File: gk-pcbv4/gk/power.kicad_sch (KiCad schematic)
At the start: 36 parts, among them J1 Conn_01x02, J2 Conn_01x02, Q1 DMN62D0U, Q2 2N7002, U1 STPMIC25B JC Module, U2 BQ24075RGT (_not_ BQ24075*T*R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, U3 MAX17048, U4 INA236[AB]IDDFR

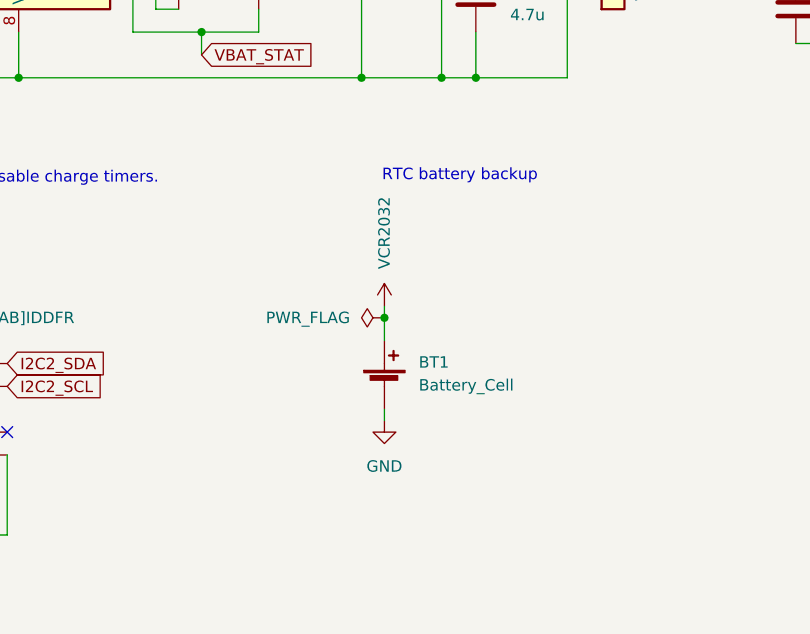
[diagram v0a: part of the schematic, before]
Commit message: add v2 controls board
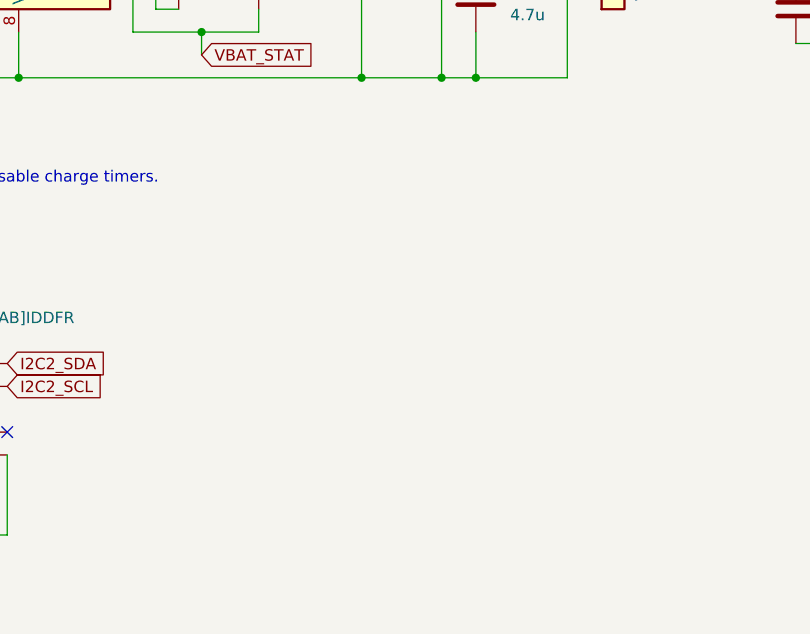
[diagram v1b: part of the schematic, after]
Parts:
- removed BT1: Battery_Cell, Battery:BatteryHolder_Keystone_3002_1x2032, symbol Device:Battery_Cell
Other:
- note removed: "RTC battery backup"

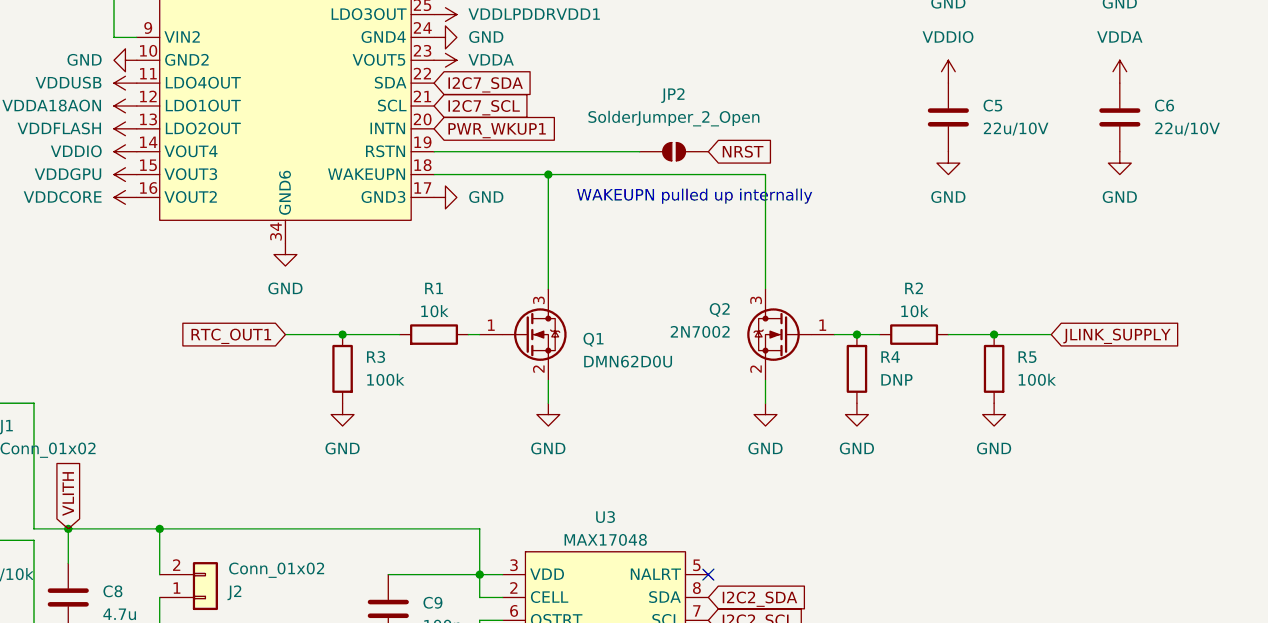
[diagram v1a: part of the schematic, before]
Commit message: Remove wakeupn mosfets in schematic
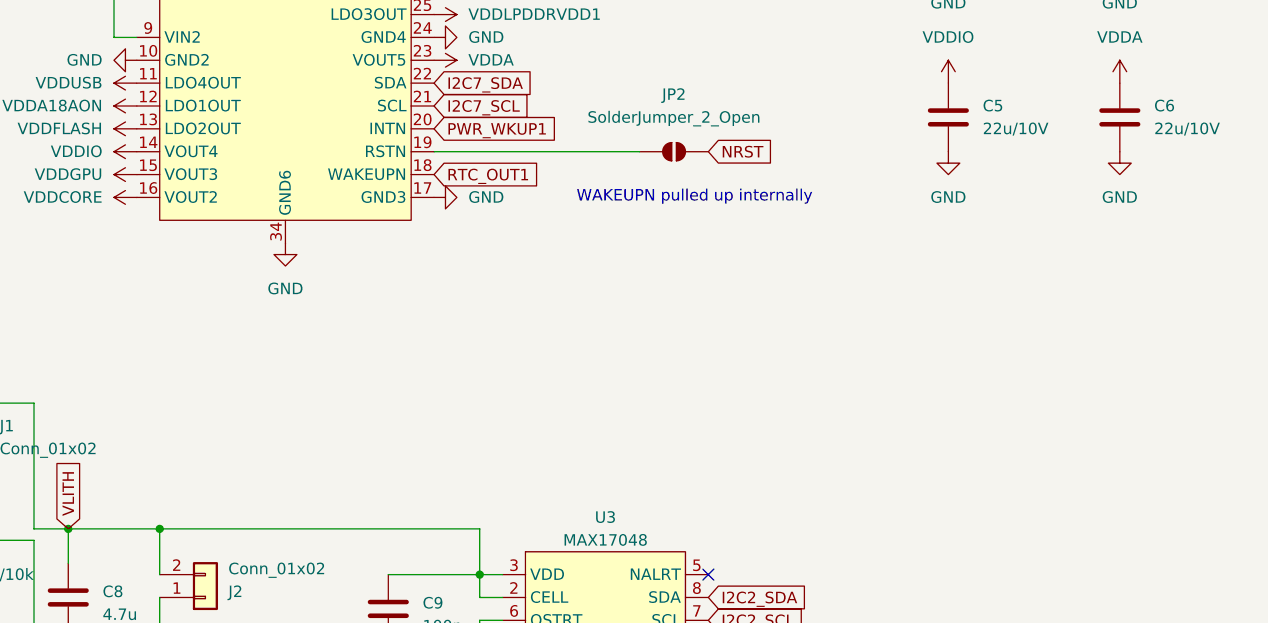
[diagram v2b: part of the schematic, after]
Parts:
- removed Q1: DMN62D0U, Package_TO_SOT_SMD:SOT-23, symbol Transistor_FET:2N7002
- removed Q2: 2N7002, Package_TO_SOT_SMD:SOT-23, symbol Transistor_FET:2N7002
- removed R1, R2: 10k, Resistor_SMD:R_0603_1608Metric, symbol Device:R
- removed R3, R5: 100k, Resistor_SMD:R_0603_1608Metric, symbol Device:R
- removed R4: DNP, Resistor_SMD:R_0603_1608Metric, symbol Device:R
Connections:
- net RTC_OUT1: now also U1.18 (WAKEUPN)

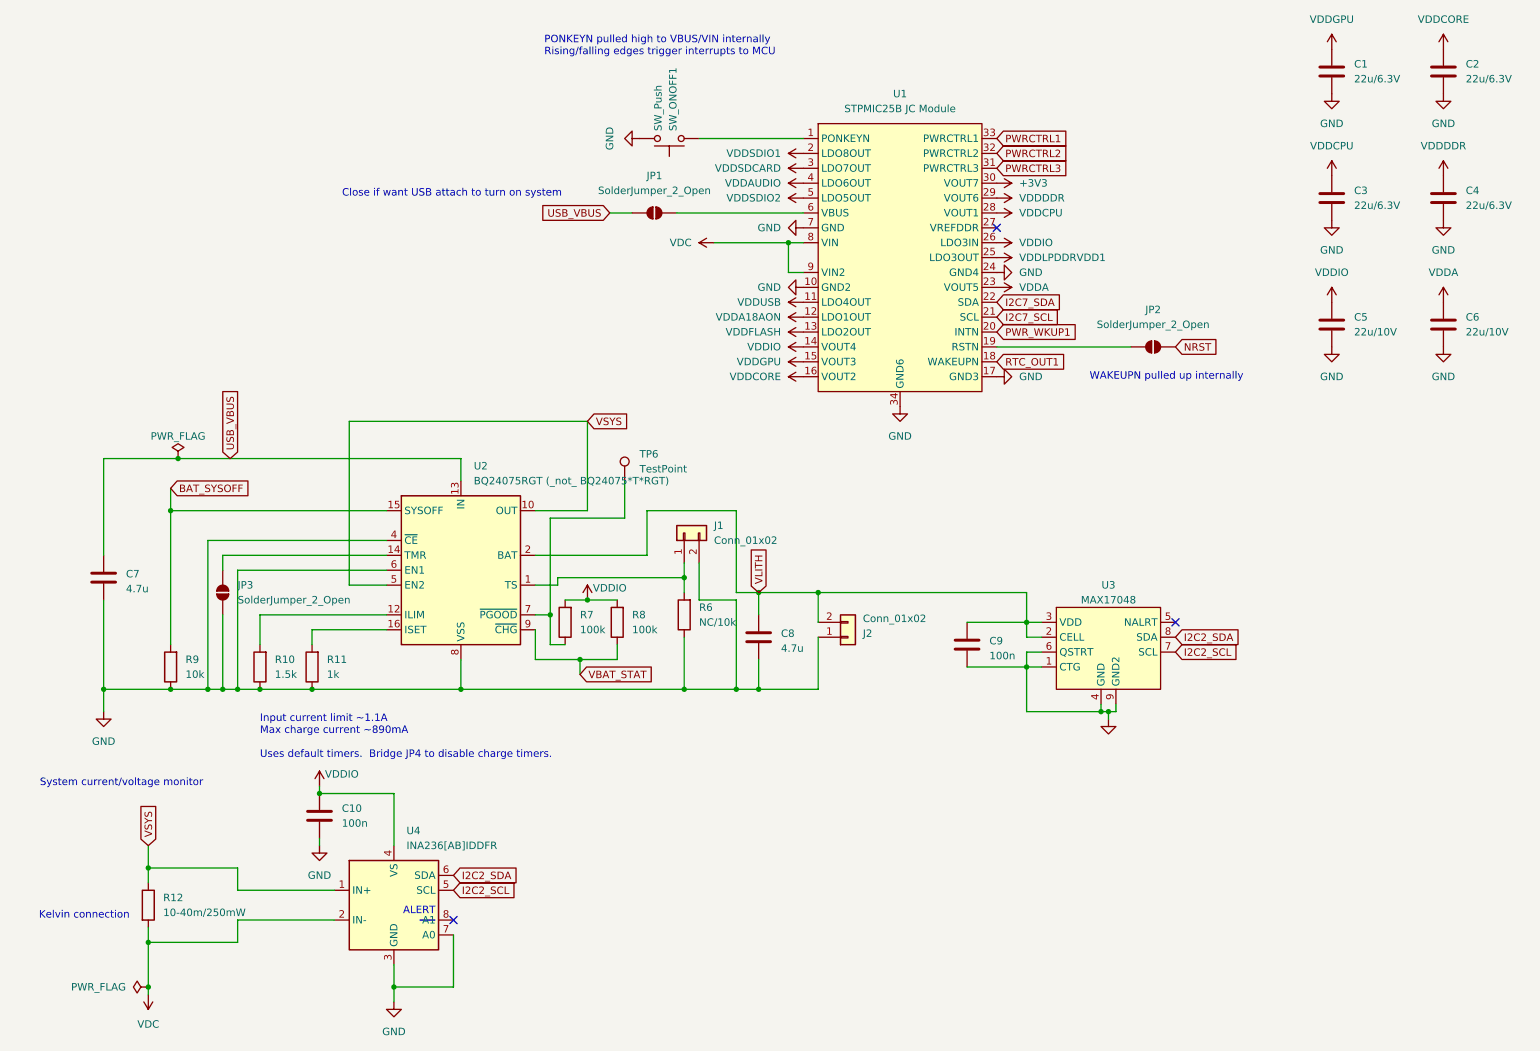
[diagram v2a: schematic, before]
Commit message: remove solder bridges
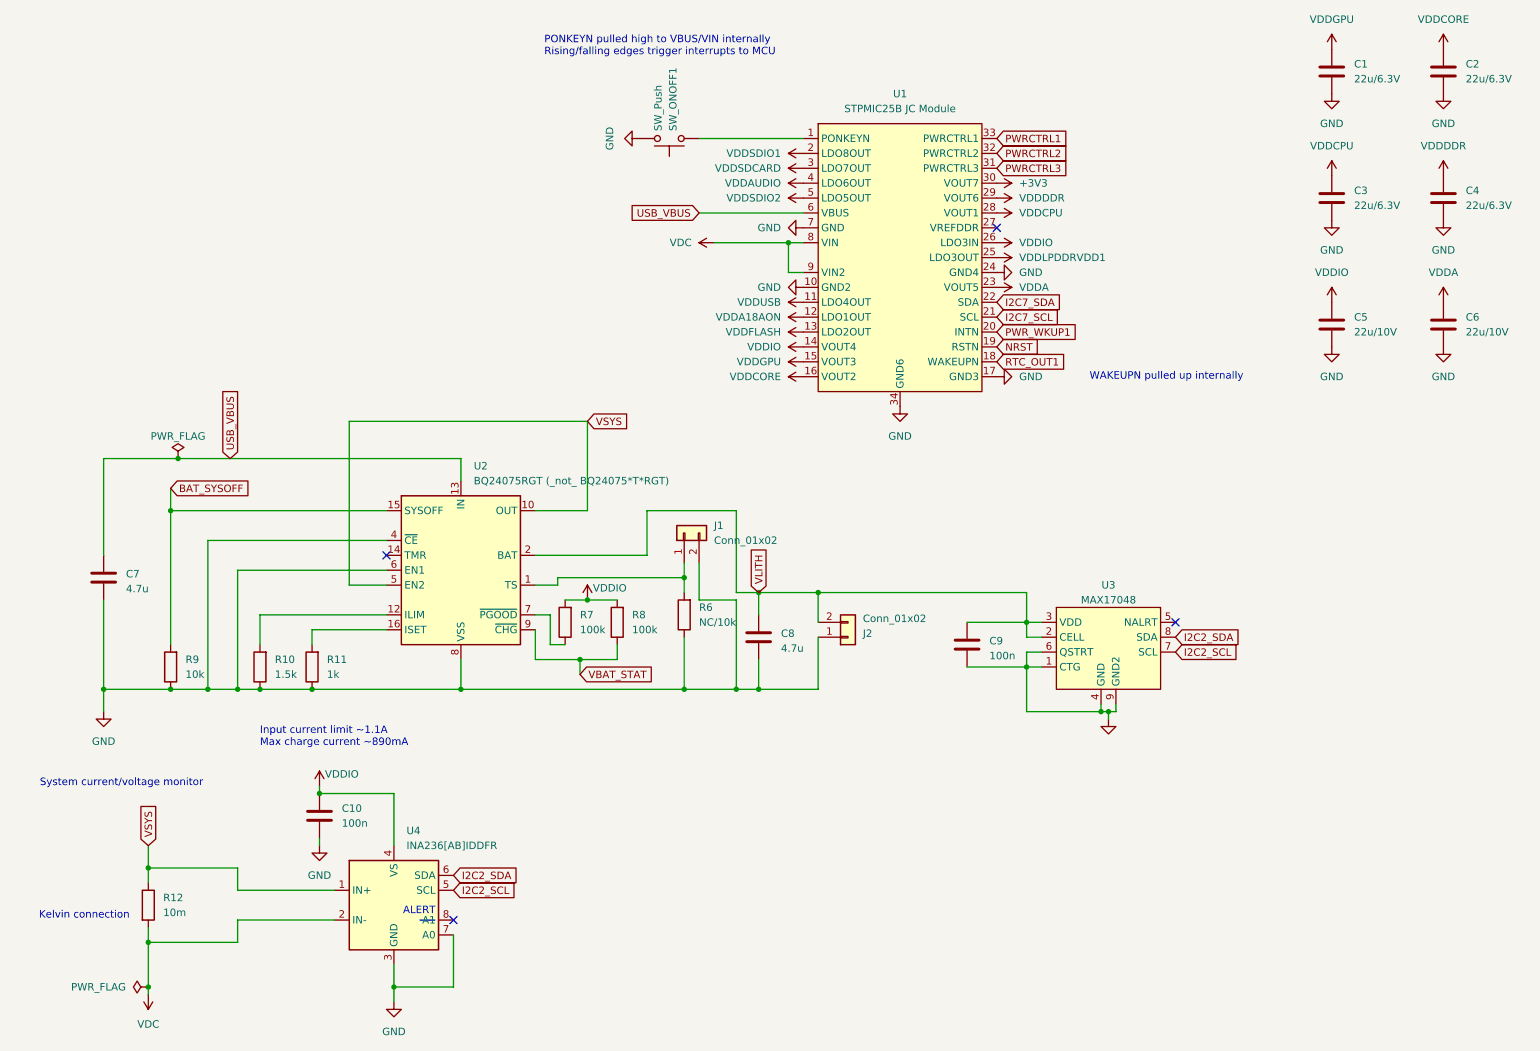
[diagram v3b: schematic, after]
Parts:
- removed JP1, JP2: SolderJumper_2_Open, Jumper:SolderJumper-2_P1.3mm_Open_TrianglePad1.0x1.5mm, symbol Jumper:SolderJumper_2_Open
- removed JP3: SolderJumper_2_Open, Jumper:SolderJumper-2_P1.3mm_Open_Pad1.0x1.5mm, symbol Jumper:SolderJumper_2_Open
- removed TP6: TestPoint, TestPoint:TestPoint_Pad_D1.0mm, symbol Connector:TestPoint
- R12: value 10-40m/250mW -> 10m
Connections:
- net NRST: now also U1.19 (RSTN)
- net USB_VBUS: now also U1.6 (VBUS)
- no-connect marks 3 -> 4
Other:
- note added: "Input current limit ~1.1A Max charge current ~890mA"
- note removed: "Close if want USB attach to turn on system"
- note removed: "Input current limit ~1.1A Max charge current ~890mA Uses default timers. Bridge JP4 to disable charge timers."

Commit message: turn back battery connectors sideways add notch for battery cables looping round from front
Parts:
- J1: footprint Connector_JST:JST_XH_B2B-XH-A_1x02_P2.50mm_Vertical -> Connector_JST:JST_XH_S2B-XH-A_1x02_P2.50mm_Horizontal
- J2: footprint Connector_JST:JST_PH_B2B-PH-K_1x02_P2.00mm_Vertical -> Connector_JST:JST_PH_S2B-PH-K_1x02_P2.00mm_Horizontal
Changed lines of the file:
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@@
 			)
 		)
-		(property "Footprint" "Connector_JST:JST_PH_B2B-PH-K_1x02_P2.00mm_Vertical"
+		(property "Footprint" "Connector_JST:JST_PH_S2B-PH-K_1x02_P2.00mm_Horizontal"
 			(at 158.75 121.92 0)
 			(effects
@@
 			)
 		)
-		(property "Footprint" "Connector_JST:JST_XH_B2B-XH-A_1x02_P2.50mm_Vertical"
+		(property "Footprint" "Connector_JST:JST_XH_S2B-XH-A_1x02_P2.50mm_Horizontal"
 			(at 130.81 104.14 0)
 			(effects

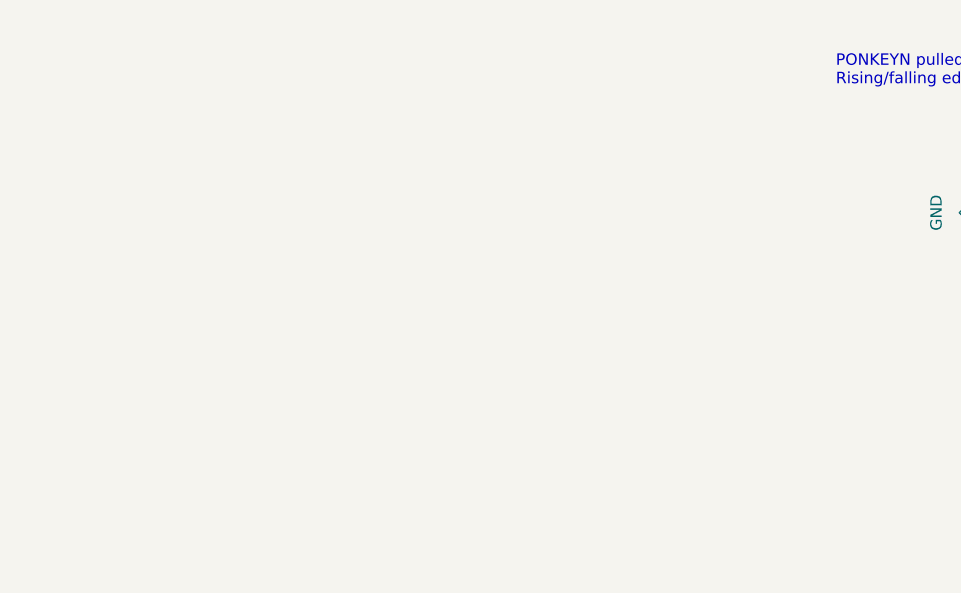
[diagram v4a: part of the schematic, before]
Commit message: add test points to power planes
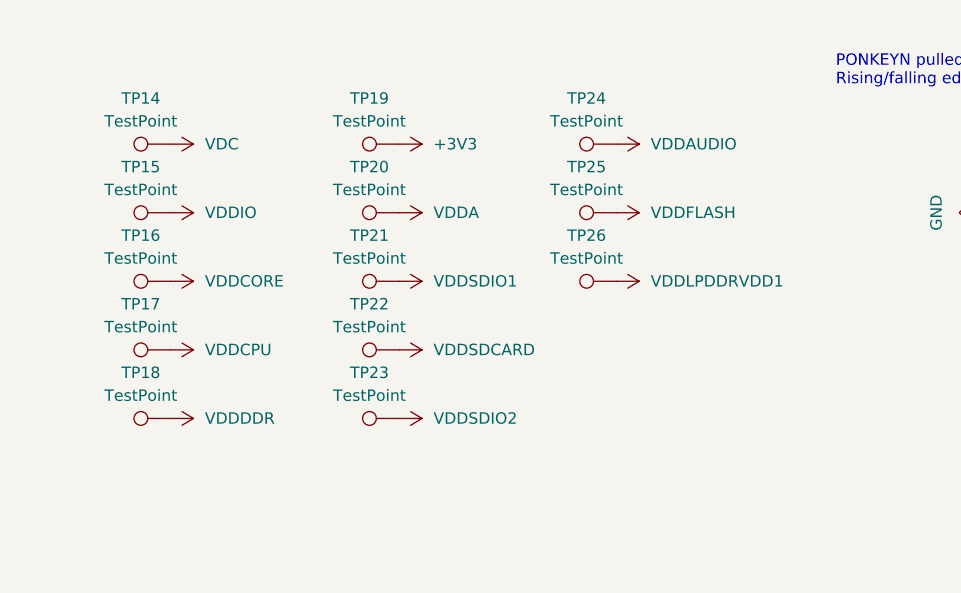
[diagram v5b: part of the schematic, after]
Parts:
- added TP14, TP15, TP16, TP17, TP18, TP19, TP20, TP21, TP22, TP23, TP24, TP25, TP26: TestPoint, TestPoint:TestPoint_Pad_D1.0mm, symbol Connector:TestPoint
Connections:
- net +3V3: now also TP19.1
- net VDC: now also TP14.1
- net VDDA: now also TP20.1
- net VDDAUDIO: now also TP24.1
- net VDDCORE: now also TP16.1
- net VDDCPU: now also TP17.1
- net VDDDDR: now also TP18.1
- net VDDFLASH: now also TP25.1
- net VDDIO: now also TP15.1
- net VDDLPDDRVDD1: now also TP26.1
- net VDDSDCARD: now also TP22.1
- net VDDSDIO1: now also TP21.1
- net VDDSDIO2: now also TP23.1
